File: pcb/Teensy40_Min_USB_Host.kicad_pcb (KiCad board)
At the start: 2 copper layers, 17.8 x 45.7 mm, 16 parts, among them J1 USB_A, J2 Conn_01x14, J3 Conn_01x14, U1 TPD3S014, U2 Teensy4.0

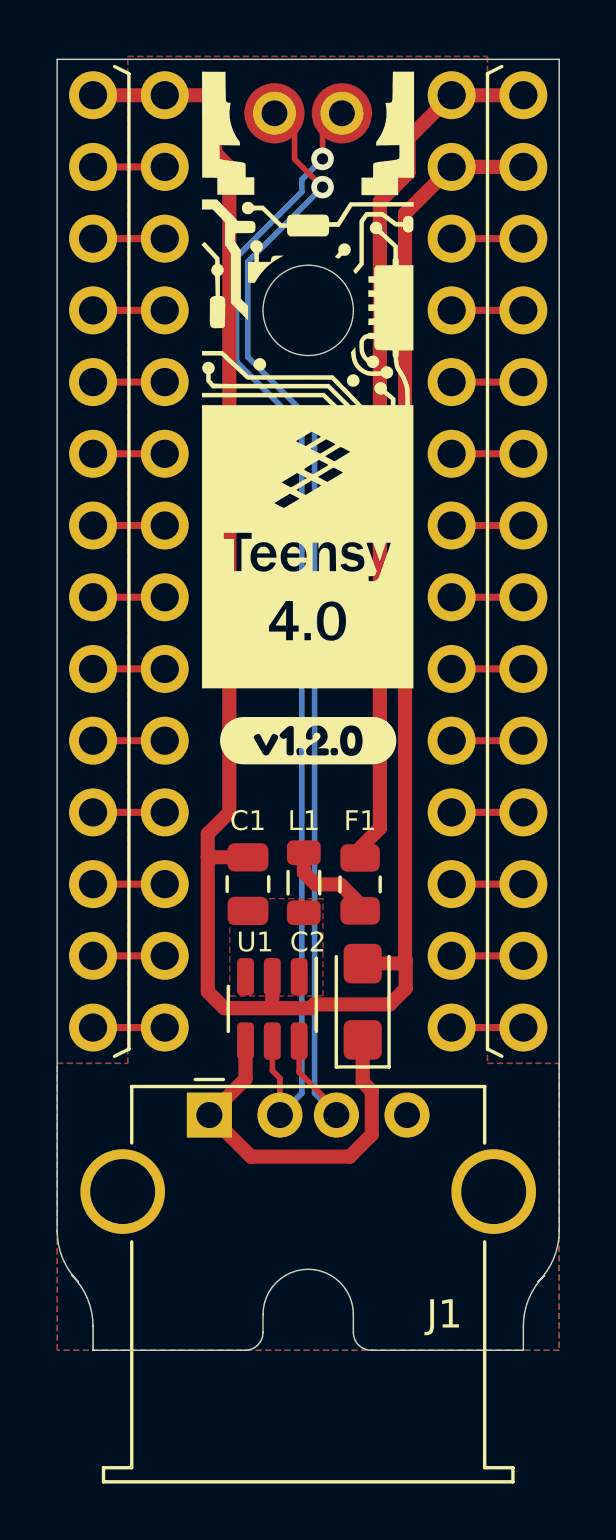
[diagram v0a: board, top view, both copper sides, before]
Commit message: Flip current limiter horizontal positions
This provides much better routing of the VBUS net, which can go directly between U1 and C2 instead of having to route around the USB port pins.
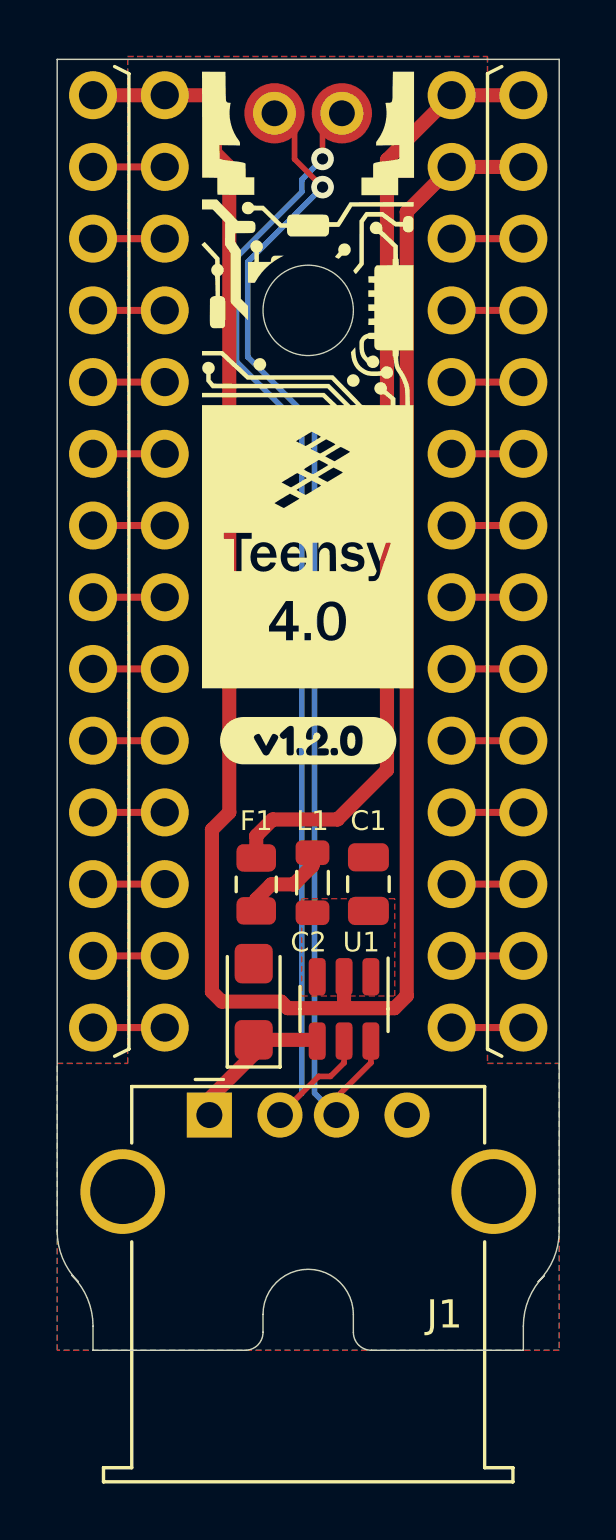
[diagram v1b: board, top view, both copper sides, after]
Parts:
- moved C1 4.27 mm to (152.0, 110.5)
- moved C2 3.86 mm to (147.9, 114.7)
- moved F1 3.68 mm to (148.0, 110.5)
- moved U1 2.54 mm to (151.1, 114.9)
- moved L1 0.30 mm to (150.0, 110.4)
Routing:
- net VBUS: track 13.2 -> 5.58 mm
- net GND: track 80.4 -> 77.5 mm
- net VCC: track 30.9 -> 33.8 mm
- net /D-: track 41.0 -> 42.1 mm

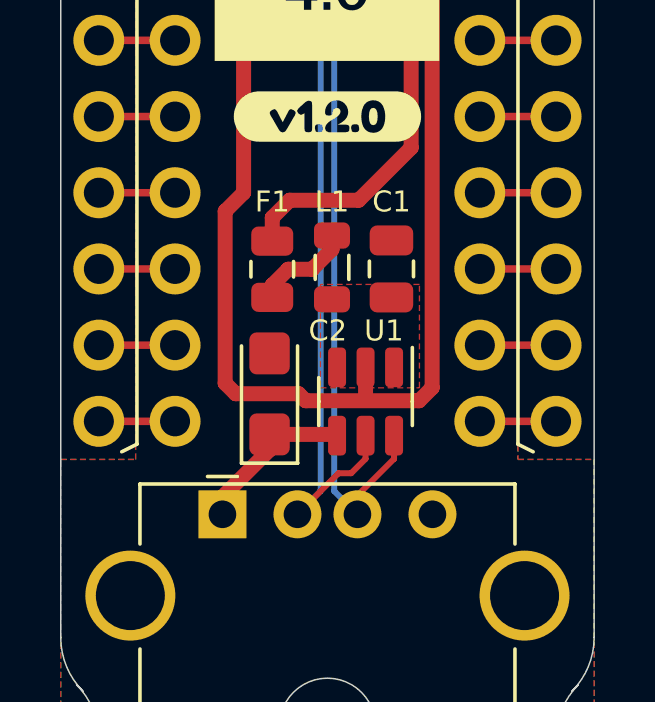
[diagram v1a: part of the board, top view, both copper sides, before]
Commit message: Center current limiting circuit block
"Center" being a rough estimate.

Man these are huge diffs for such a minor change... those filled zones are no joke.
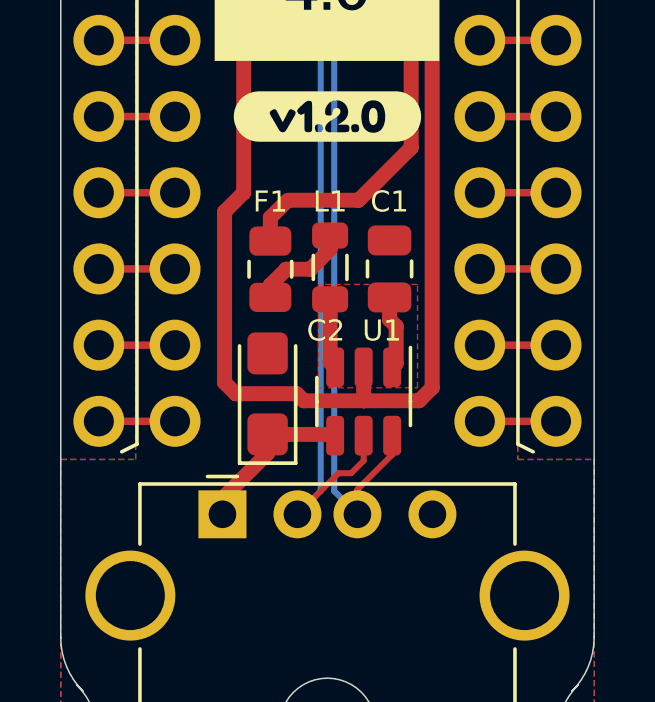
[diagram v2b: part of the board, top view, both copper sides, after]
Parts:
- moved F1 0.06 mm to (148.0, 110.5)
- moved L1 0.06 mm to (149.9, 110.4)
- moved U1 0.06 mm to (151.1, 114.9)
- moved C1 0.06 mm to (151.9, 110.5)
- moved C2 0.06 mm to (147.9, 114.7)
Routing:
- net /VIN: track 0.00 -> 4.82 mm
